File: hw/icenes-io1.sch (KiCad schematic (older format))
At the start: 49 parts, among them J3 Conn_02x11_Odd_Even, U4 iCE40HX8K-CT256, U8 SN74LVC1404, U9 SN74LVC1404, Y1 21.47727MHz, Y2 26.601712MHz

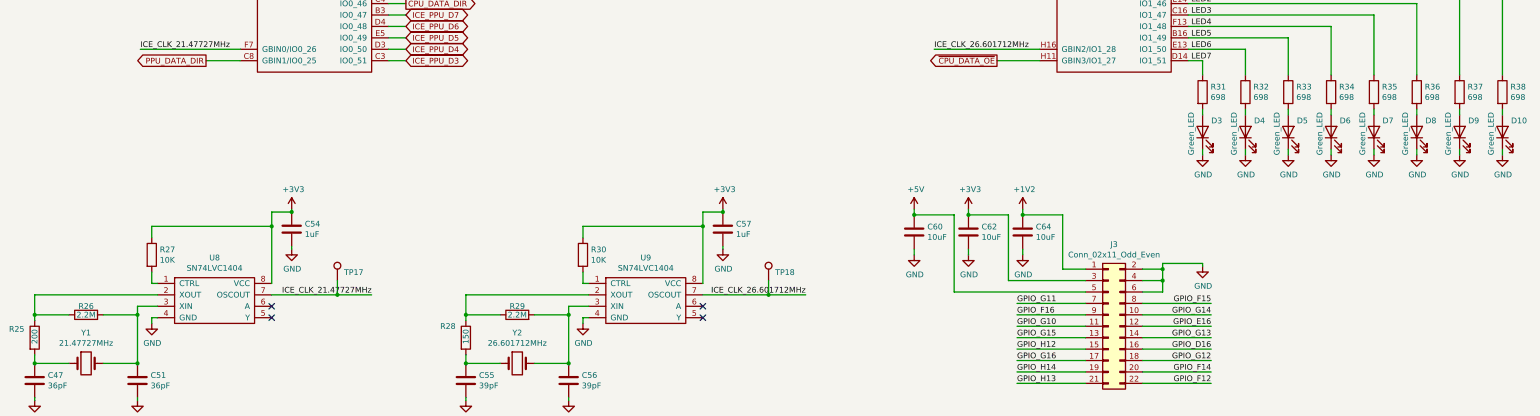
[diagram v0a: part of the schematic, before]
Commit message: Added voltage range in Vin lable (+5V to +10V).
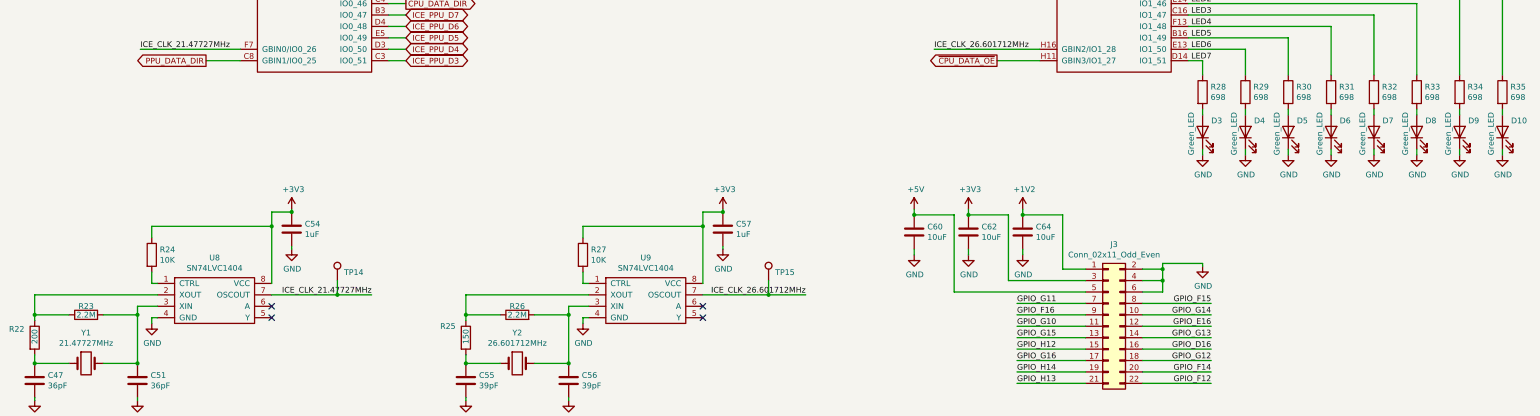
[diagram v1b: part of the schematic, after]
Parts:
- renumbered R25 to R22, R26 to R23, R27 to R24, R28 to R25, R29 to R26, R30 to R27, R31 to R28, R32 to R29, R33 to R30, R34 to R31, R35 to R32, R36 to R33, R37 to R34, R38 to R35, TP17 to TP14, TP18 to TP15
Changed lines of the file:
@@
 $EndComp
 $Comp
-L icenes-library:R698 R31
+L icenes-library:R698 R28
 U 1 1 5D435DC8
 P 11275 7075
-F 0 "R31" V 11229 7145 50  0000 L CNN
+F 0 "R28" V 11229 7145 50  0000 L CNN
 F 1 "R698" H 11275 6975 50  0001 C CNN
 F 2 "Resistor_SMD:R_0603_1608Metric_Pad1.05x0.95mm_HandSolder" V 11275 7075 50  0001 C CNN
@@
 $EndComp
 $Comp
-L icenes-library:R698 R32
+L icenes-library:R698 R29
 U 1 1 5D49EA53
 P 11650 7075
-F 0 "R32" V 11604 7145 50  0000 L CNN
+F 0 "R29" V 11604 7145 50  0000 L CNN
 F 1 "R698" H 11650 6975 50  0001 C CNN
 F 2 "Resistor_SMD:R_0603_1608Metric_Pad1.05x0.95mm_HandSolder" V 11650 7075 50  0001 C CNN
@@
 $EndComp
 $Comp
-L icenes-library:R698 R33
+L icenes-library:R698 R30
 U 1 1 5D4AAC01
 P 12025 7075
-F 0 "R33" V 11979 7145 50  0000 L CNN
+F 0 "R30" V 11979 7145 50  0000 L CNN
 F 1 "R698" H 12025 6975 50  0001 C CNN
 F 2 "Resistor_SMD:R_0603_1608Metric_Pad1.05x0.95mm_HandSolder" V 12025 7075 50  0001 C CNN
@@
 $EndComp
 $Comp
-L icenes-library:R698 R34
+L icenes-library:R698 R31
 U 1 1 5D4B0BF6
 P 12400 7075
-F 0 "R34" V 12354 7145 50  0000 L CNN
+F 0 "R31" V 12354 7145 50  0000 L CNN
 F 1 "R698" H 12400 6975 50  0001 C CNN
 F 2 "Resistor_SMD:R_0603_1608Metric_Pad1.05x0.95mm_HandSolder" V 12400 7075 50  0001 C CNN
@@
 $EndComp
 $Comp
-L icenes-library:R698 R35
+L icenes-library:R698 R32
 U 1 1 5D4B6CEA
 P 12775 7075
-F 0 "R35" V 12729 7145 50  0000 L CNN
+F 0 "R32" V 12729 7145 50  0000 L CNN
 F 1 "R698" H 12775 6975 50  0001 C CNN
 F 2 "Resistor_SMD:R_0603_1608Metric_Pad1.05x0.95mm_HandSolder" V 12775 7075 50  0001 C CNN
@@
 $EndComp
 $Comp
-L icenes-library:R698 R36
+L icenes-library:R698 R33
 U 1 1 5D4BD4B7
 P 13150 7075
-F 0 "R36" V 13104 7145 50  0000 L CNN
+F 0 "R33" V 13104 7145 50  0000 L CNN
 F 1 "R698" H 13150 6975 50  0001 C CNN
 F 2 "Resistor_SMD:R_0603_1608Metric_Pad1.05x0.95mm_HandSolder" V 13150 7075 50  0001 C CNN
@@
 $EndComp
 $Comp
-L icenes-library:R698 R37
+L icenes-library:R698 R34
 U 1 1 5D4C38D7
 P 13525 7075
-F 0 "R37" V 13479 7145 50  0000 L CNN
+F 0 "R34" V 13479 7145 50  0000 L CNN
 F 1 "R698" H 13525 6975 50  0001 C CNN
 F 2 "Resistor_SMD:R_0603_1608Metric_Pad1.05x0.95mm_HandSolder" V 13525 7075 50  0001 C CNN
@@
 $EndComp
 $Comp
-L icenes-library:R698 R38
+L icenes-library:R698 R35
 U 1 1 5D4C971E
 P 13900 7075
-F 0 "R38" V 13854 7145 50  0000 L CNN
+F 0 "R35" V 13854 7145 50  0000 L CNN
 F 1 "R698" H 13900 6975 50  0001 C CNN
 F 2 "Resistor_SMD:R_0603_1608Metric_Pad1.05x0.95mm_HandSolder" V 13900 7075 50  0001 C CNN
@@
 	3125 8250 3125 8750
 $Comp
-L icenes-library:R10K R27
+L icenes-library:R10K R24
 U 1 1 5D74F353
 P 2075 8500
-F 0 "R27" V 2029 8570 50  0000 L CNN
+F 0 "R24" V 2029 8570 50  0000 L CNN
 F 1 "R10K" H 2075 8400 50  0001 C CNN
 F 2 "Resistor_SMD:R_0603_1608Metric_Pad1.05x0.95mm_HandSolder" V 2075 8500 50  0001 C CNN
@@
 Connection ~ 1950 9450
 $Comp
-L icenes-library:R200 R25
+L icenes-library:R200 R22
 U 1 1 5DA45067
 P 1050 9225
-F 0 "R25" V 975 9000 50  0000 L CNN
+F 0 "R22" V 975 9000 50  0000 L CNN
 F 1 "R200" H 1050 9125 50  0001 C CNN
 F 2 "Resistor_SMD:R_0603_1608Metric_Pad1.05x0.95mm_HandSolder" V 1050 9225 50  0001 C CNN
@@
 $EndComp
 $Comp
-L icenes-library:R2.2M R26
+L icenes-library:R2.2M R23
 U 1 1 5DA4708D
 P 1500 9025
-F 0 "R26" H 1500 9100 50  0000 C CNN
+F 0 "R23" H 1500 9100 50  0000 C CNN
 F 1 "R2.2M" H 1500 8925 50  0001 C CNN
 F 2 "Resistor_SMD:R_0603_1608Metric_Pad1.05x0.95mm_HandSolder" V 1500 9025 50  0001 C CNN
@@
 	3700 8850 4000 8850
 $Comp
-L icenes-library:TestPoint TP17
+L icenes-library:TestPoint TP14
 U 1 1 5DB07242
 P 3700 8725
-F 0 "TP17" H 3758 8797 50  0000 L CNN
+F 0 "TP14" H 3758 8797 50  0000 L CNN
 F 1 "TestPoint" H 3700 8925 50  0001 C CNN
 F 2 "TestPoint:TestPoint_Pad_D1.0mm" H 3900 8725 50  0001 C CNN
@@
 	6900 8250 6900 8750
 $Comp
-L icenes-library:R10K R30
+L icenes-library:R10K R27
 U 1 1 5DB221D0
 P 5850 8500
-F 0 "R30" V 5804 8570 50  0000 L CNN
+F 0 "R27" V 5804 8570 50  0000 L CNN
 F 1 "R10K" H 5850 8400 50  0001 C CNN
 F 2 "Resistor_SMD:R_0603_1608Metric_Pad1.05x0.95mm_HandSolder" V 5850 8500 50  0001 C CNN
@@
 Connection ~ 4825 9025
 $Comp
-L icenes-library:R2.2M R29
+L icenes-library:R2.2M R26
 U 1 1 5DB2222B
 P 5275 9025
-F 0 "R29" H 5275 9100 50  0000 C CNN
+F 0 "R26" H 5275 9100 50  0000 C CNN
 F 1 "R2.2M" H 5275 8925 50  0001 C CNN
 F 2 "Resistor_SMD:R_0603_1608Metric_Pad1.05x0.95mm_HandSolder" V 5275 9025 50  0001 C CNN
@@
 Connection ~ 7475 8850
 $Comp
-L icenes-library:TestPoint TP18
+L icenes-library:TestPoint TP15
 U 1 1 5DB22244
 P 7475 8725
-F 0 "TP18" H 7533 8797 50  0000 L CNN
+F 0 "TP15" H 7533 8797 50  0000 L CNN
 F 1 "TestPoint" H 7475 8925 50  0001 C CNN
 F 2 "TestPoint:TestPoint_Pad_D1.0mm" H 7675 8725 50  0001 C CNN
@@
 Connection ~ 5725 9450
 $Comp
-L icenes-library:R150 R28
+L icenes-library:R150 R25
 U 1 1 5DB3EF0F
 P 4825 9225
-F 0 "R28" V 4725 9000 50  0000 L CNN
+F 0 "R25" V 4725 9000 50  0000 L CNN
 F 1 "R150" H 4825 9125 50  0001 C CNN
 F 2 "Resistor_SMD:R_0603_1608Metric_Pad1.05x0.95mm_HandSolder" V 4825 9225 50  0001 C CNN

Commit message: Layout.
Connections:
- net +1V2: now also C60.1, J3.5 (Pin_5); no longer C64.1, J3.1 (Pin_1)
- net +5V: now also C64.1, J3.1 (Pin_1); no longer C60.1, J3.5 (Pin_5)
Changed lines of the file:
@@
 L power:+1V2 #PWR076
 U 1 1 5D76E658
+P 8750 8100
+F 0 "#PWR076" H 8750 7950 50  0001 C CNN
+F 1 "+1V2" H 8765 8273 50  0000 C CNN
+F 2 "" H 8750 8100 50  0001 C CNN
+F 3 "" H 8750 8100 50  0001 C CNN
+	1    8750 8100
+	1    0    0    -1
+$EndComp
+$Comp
+L power:+5V #PWR071
+U 1 1 5D76F52B
 P 9700 8100
-F 0 "#PWR076" H 9700 7950 50  0001 C CNN
-F 1 "+1V2" H 9715 8273 50  0000 C CNN
+F 0 "#PWR071" H 9700 7950 50  0001 C CNN
+F 1 "+5V" H 9715 8273 50  0000 C CNN
 F 2 "" H 9700 8100 50  0001 C CNN
 F 3 "" H 9700 8100 50  0001 C CNN
 	1    9700 8100
-	1    0    0    -1
-$EndComp
-$Comp
-L power:+5V #PWR071
-U 1 1 5D76F52B
-P 8750 8100
-F 0 "#PWR071" H 8750 7950 50  0001 C CNN
-F 1 "+5V" H 8765 8273 50  0000 C CNN
-F 2 "" H 8750 8100 50  0001 C CNN
-F 3 "" H 8750 8100 50  0001 C CNN
-	1    8750 8100
 	1    0    0    -1
 $EndComp
@@
 Wire Wire Line
 	2300 3550 2300 3500
+Text Label 1050 1900 0    50   ~ 0
+VCCIO0_3V3
+Text Label 8050 1900 0    50   ~ 0
+VCCIO1_3V3
+Text Label 1950 3100 0    50   ~ 0
+VCCPLL0_1V2
 $EndSCHEMATC

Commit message: Layout.
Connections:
- net ICE_CLK_21.47727MHz: now also U4.H16 (GBIN2/IO1_28); no longer U4.F7 (GBIN0/IO0_26)
- net ICE_CLK_26.601712MHz: now also U4.F7 (GBIN0/IO0_26); no longer U4.H16 (GBIN2/IO1_28)
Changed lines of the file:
@@
 Connection ~ 3300 8125
 Connection ~ 3125 8250
-Text Label 1975 6700 0    50   ~ 0
+Text Label 8975 6700 0    50   ~ 0
 ICE_CLK_21.47727MHz
 Wire Wire Line
-	1975 6700 2850 6700
+	8975 6700 9850 6700
 Wire Wire Line
 	1050 8850 2125 8850
@@
 Wire Wire Line
 	7475 8850 7800 8850
-Text Label 8925 6700 0    50   ~ 0
+Text Label 1925 6700 0    50   ~ 0
 ICE_CLK_26.601712MHz
 Wire Wire Line
-	8925 6700 9850 6700
-Text GLabel 2550 6800 0    50   Output ~ 0
+	1925 6700 2850 6700
+Text GLabel 2500 6800 0    50   Output ~ 0
 PPU_DATA_DIR
-Wire Wire Line
-	2550 6800 2850 6800
-Text GLabel 9475 6800 0    50   Output ~ 0
+Text GLabel 9525 6800 0    50   Output ~ 0
 ~CPU_DATA_OE
-Wire Wire Line
-	9475 6800 9850 6800
 $Comp
 L power:PWR_FLAG #FLG?
@@
 Text Label 1950 3100 0    50   ~ 0
 VCCPLL0_1V2
+Wire Wire Line
+	2500 6800 2850 6800
+Wire Wire Line
+	9850 6800 9525 6800
 $EndSCHEMATC

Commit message: Layout.
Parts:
- removed C60, C62, C64: C10uF, Capacitor_SMD:C_0603_1608Metric_Pad1.05x0.95mm_HandSolder, symbol icenes-library:C10uF
- removed J3: Conn_02x11_Odd_Even, Connector_PinSocket_2.54mm:PinSocket_2x11_P2.54mm_Vertical, symbol icenes-library:Conn_02x11_Odd_Even
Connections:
- net CTSn is gone; now on net ~PPU_DATA_OE: U4.B14 (IO0_03)
- net DCDn is gone; now on net PPU_ADDR_DIR: U4.C13 (IO0_06)
- net DSRn is gone; now on net LED2: U4.E11 (IO0_05)
- net DTRn is gone; now on net ~PPU_ADDR_OE: U4.C12 (IO0_04)
- net GPIO_D16 is gone; now on net ICE_CPU_D2: U4.D16 (IO1_40)
- net GPIO_E16 is gone; now on net ICE_CPU_D1: U4.E16 (IO1_38)
- net GPIO_F12 is gone; now on net ICE_M2: U4.F12 (IO1_43)
- net GPIO_F14 is gone; now on net CPU_DATA_DIR: U4.F14 (IO1_42)
- net GPIO_F15 is gone; now on net ICE_CIRAM_A10: U4.F15 (IO1_36)
- net GPIO_F16 is gone; now on net ICE_CPU_D0: U4.F16 (IO1_34)
- net GPIO_G10 is gone; now on net ICE_PPU_D3: U4.G10 (IO1_33)
- net GPIO_G11 is gone; now on net ICE_PPU_D2: U4.G11 (IO1_35)
- net GPIO_G12 is gone; now on net ICE_SYSTEM_CLK: U4.G12 (IO1_41)
- net GPIO_G13 is gone; now on net ICE_CICtoPak: U4.G13 (IO1_39)
- net GPIO_G15 is gone; now on net ~ICE_CIRAM_CE: U4.G15 (IO1_32)
- net GPIO_G16 is gone; now on net ~CPU_DATA_OE: U4.G16 (IO1_30)
- net GPIO_H13 is gone; now on net ICE_CIC_CLK: U4.H13 (IO1_26)
- net GPIO_H14 is gone; now on net ~ICE_IRQ: U4.H14 (IO1_29)
- net RS232_RX_TTL is gone; now on net ICE_PPU_D1: U4.C14 (IO0_00)
- net RS232_TX_TTL is gone; now on net ICE_PPU_D0: U4.B15 (IO0_01)
- net RTSn is gone; now on net LED1: U4.D13 (IO0_02)
- net CPU_ADDR_DIR: now also U4.D7 (IO0_35); no longer U4.D8 (IO0_28)
- net CPU_DATA_DIR: no longer U4.C4 (IO0_46)
- net ICE_CIC_CLK: no longer U4.K13 (IO1_17)
- net ICE_CICtoMB: now also U4.E13 (IO1_50); no longer U4.J14 (IO1_22)
- net ICE_CICtoPak: no longer U4.K14 (IO1_18)
- net ICE_CIRAM_A10: no longer U4.J16 (IO1_25)
- net ICE_CPU_A0: now also U4.B8 (IO0_29); no longer U4.A1 (IO0_44)
- net ICE_CPU_A1: now also U4.B7 (IO0_32); no longer U4.D5 (IO0_43)
- net ICE_CPU_A10: now also U4.B5 (IO0_39); no longer U4.C6 (IO0_34)
- net ICE_CPU_A11: now also U4.C3 (IO0_51); no longer U4.B6 (IO0_33)
- net ICE_CPU_A12: now also U4.B4 (IO0_41); no longer U4.B7 (IO0_32)
- net ICE_CPU_A13: now also U4.A2 (IO0_42); no longer U4.C7 (IO0_31)
- net ICE_CPU_A14: now also U4.D3 (IO0_50); no longer U4.A7 (IO0_30)
- net ICE_CPU_A2: now also U4.D6 (IO0_37); no longer U4.A2 (IO0_42)
- net ICE_CPU_A3: now also U4.A7 (IO0_30); no longer U4.B4 (IO0_41)
- net ICE_CPU_A4: now also U4.B6 (IO0_33); no longer U4.E6 (IO0_40)
- net ICE_CPU_A5: now also U4.C5 (IO0_45); no longer U4.B5 (IO0_39)
- net ICE_CPU_A6: now also U4.C4 (IO0_46); no longer U4.A5 (IO0_38)
- net ICE_CPU_A7: now also U4.A6 (IO0_36); no longer U4.D6 (IO0_37)
- net ICE_CPU_A8: now also U4.B3 (IO0_47); no longer U4.A6 (IO0_36)
- net ICE_CPU_A9: now also U4.A5 (IO0_38); no longer U4.D7 (IO0_35)
- net ICE_CPU_D0: no longer U4.L14 (IO1_10)
- net ICE_CPU_D1: no longer U4.L13 (IO1_09)
- net ICE_CPU_D2: no longer U4.N16 (IO1_08)
- net ICE_CPU_D3: now also U4.E14 (IO1_46); no longer U4.L12 (IO1_07)
- net ICE_CPU_D4: now also U4.D14 (IO1_51); no longer U4.M14 (IO1_06)
- net ICE_CPU_D5: now also U4.D15 (IO1_44); no longer U4.M13 (IO1_05)
- net ICE_CPU_D6: now also U4.C16 (IO1_47); no longer U4.P16 (IO1_04)
- net ICE_CPU_D7: now also U4.B16 (IO1_49); no longer U4.P15 (IO1_03)
- net ICE_CPU_RW: now also U4.A1 (IO0_44); no longer U4.B8 (IO0_29)
- net ICE_M2: no longer U4.M15 (IO1_14)
- net ICE_PPU_A0: now also U4.B12 (IO0_13); no longer U4.E10 (IO0_10)
- net ICE_PPU_A1: now also U4.B11 (IO0_15); no longer U4.C11 (IO0_11)
- net ICE_PPU_A11: now also U4.B9 (IO0_27); no longer U4.E9 (IO0_21)
- net ICE_PPU_A2: now also U4.E9 (IO0_21); no longer U4.D11 (IO0_12)
- net ICE_PPU_A3: now also U4.D8 (IO0_28); no longer U4.B12 (IO0_13)
- net ICE_PPU_A4: now also U4.E6 (IO0_40); no longer U4.B10 (IO0_14)
- net ICE_PPU_A5: now also U4.C11 (IO0_11); no longer U4.B11 (IO0_15)
- net ICE_PPU_A7: now also U4.A11 (IO0_18); no longer U4.A10 (IO0_17)
- net ICE_PPU_A8: now also U4.B10 (IO0_14); no longer U4.A11 (IO0_18)
- net ICE_PPU_A9: now also U4.A10 (IO0_17); no longer U4.D10 (IO0_19)
- net ICE_PPU_D0: no longer U4.P14 (IO1_02)
- net ICE_PPU_D1: no longer U4.R15 (IO1_01)
- net ICE_PPU_D2: no longer U4.R14 (IO1_00)
- net ICE_PPU_D3: no longer U4.C3 (IO0_51)
- net ICE_PPU_D4: now also U4.E10 (IO0_10); no longer U4.D3 (IO0_50)
- net ICE_PPU_D5: now also U4.F9 (IO0_24); no longer U4.E5 (IO0_49)
- net ICE_PPU_D6: now also U4.A16 (IO0_07); no longer U4.D4 (IO0_48)
- net ICE_PPU_D7: now also U4.A15 (IO0_08); no longer U4.B3 (IO0_47)
- net ICE_SYSTEM_CLK: no longer U4.J10 (IO1_13)
- net LED0: now also U4.F11 (IO1_45); no longer U4.D15 (IO1_44)
- net LED1: no longer U4.F11 (IO1_45)
- net LED2: no longer U4.E14 (IO1_46)
- net LED3: now also U4.D11 (IO0_12); no longer U4.C16 (IO1_47)
- net LED4: now also U4.D10 (IO0_19); no longer U4.F13 (IO1_48)
- net LED5: now also U4.E5 (IO0_49); no longer U4.B16 (IO1_49)
- net LED6: now also U4.D5 (IO0_43); no longer U4.E13 (IO1_50)
- net LED7: now also U4.D4 (IO0_48); no longer U4.D14 (IO1_51)
- net MISC_DIR2: now also U4.J16 (IO1_25); no longer U4.K16 (IO1_21)
- net PPU_ADDR_DIR: no longer U4.A15 (IO0_08)
- net PPU_DATA_DIR: now also U4.B13 (IO0_09); no longer U4.C8 (GBIN1/IO0_25)
- net ~CPU_ADDR_OE: now also U4.C6 (IO0_34); no longer U4.B9 (IO0_27)
- net ~CPU_DATA_OE: no longer U4.H11 (GBIN3/IO1_27)
- net ~ICE_CIC_RST: now also U4.F13 (IO1_48); no longer U4.J15 (IO1_19)
- net ~ICE_CIRAM_CE: no longer U4.J13 (IO1_24)
- net ~ICE_IRQ: no longer U4.J12 (IO1_23)
- net ~ICE_PPU_A13: now also U4.C8 (GBIN1/IO0_25); no longer U4.F9 (IO0_24)
- net ~ICE_PPU_RD: now also U4.K15 (IO1_20); no longer U4.J11 (IO1_15)
- net ~ICE_PPU_WR: now also U4.C7 (IO0_31); no longer U4.B13 (IO0_09)
- net ~ICE_ROMSEL: now also U4.K16 (IO1_21); no longer U4.L16 (IO1_16)
- net ~MISC_OE1: now also U4.L16 (IO1_16); no longer U4.K12 (IO1_11)
- net ~MISC_OE2: now also U4.J15 (IO1_19); no longer U4.K15 (IO1_20)
- net ~PPU_ADDR_OE: no longer U4.A16 (IO0_07)
- net ~PPU_DATA_OE: no longer U4.C5 (IO0_45)
- net GPIO_H12 renamed GPIO_E13
- new net GPIO_C10: U4.J10 (IO1_13)
- new net GPIO_H11: U4.H11 (GBIN3/IO1_27)
- new net GPIO_J11: U4.J11 (IO1_15)
- new net GPIO_J12: U4.J12 (IO1_23)
- new net GPIO_J13: U4.J13 (IO1_24)
- new net GPIO_J14: U4.J14 (IO1_22)
- new net GPIO_K12: U4.K12 (IO1_11)
- new net GPIO_K13: U4.K13 (IO1_17)
- new net GPIO_K14: U4.K14 (IO1_18)
- new net GPIO_L12: U4.L12 (IO1_07)
- new net GPIO_L13: U4.L13 (IO1_09)
- new net GPIO_M13: U4.M13 (IO1_05)
- new net GPIO_M14: U4.M14 (IO1_06)
- new net GPIO_M15: U4.M15 (IO1_14)
- new net GPIO_M16: U4.L14 (IO1_10)
- new net GPIO_N16: U4.N16 (IO1_08)
- new net GPIO_P14: U4.P14 (IO1_02)
- new net GPIO_P15: U4.P15 (IO1_03)
- new net GPIO_P16: U4.P16 (IO1_04)
- new net GPIO_R14: U4.R14 (IO1_00)
- new net GPIO_R15: U4.R15 (IO1_01)
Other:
- moved on the sheet: D10, D3, D4, D5, D6, D7, D8, D9, R28, R29, R30, R31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

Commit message: Layout. Added some info for the PAL crystal.
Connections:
- net GPIO_E13 renamed GPIO_H12
- net GPIO_M16 renamed GPIO_L14
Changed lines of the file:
@@
 Text Label 4750 6000 2    50   ~ 0
 LED6
-Text Label 12075 2300 2    50   ~ 0
-GPIO_P16
 Text Label 5125 3100 2    50   ~ 0
 LED3
 Text Label 11750 5400 2    50   ~ 0
 GPIO_G14
-Text Label 11750 3000 2    50   ~ 0
-GPIO_K12
-Text Label 11750 2400 2    50   ~ 0
-GPIO_M13
-Text Label 11750 2600 2    50   ~ 0
-GPIO_L12
-Text Label 11750 4100 2    50   ~ 0
-GPIO_J14
-Text Label 11750 3600 2    50   ~ 0
-GPIO_K13
-Text Label 11750 4200 2    50   ~ 0
-GPIO_J12
 Text GLabel 12000 5300 2    50   Input ~ 0
 ICE_CIRAM_A10
@@
 Wire Wire Line
 	11150 4800 11750 4800
-Text Label 11750 3300 2    50   ~ 0
-GPIO_M15
 Text Label 11750 6200 2    50   ~ 0
 LED0
-Text Label 11750 4300 2    50   ~ 0
-GPIO_J13
 Text Label 11750 3200 2    50   ~ 0
 GPIO_C10
-Text Label 11750 3700 2    50   ~ 0
-GPIO_K14
-Text Label 11750 2900 2    50   ~ 0
-GPIO_M16
-Text Label 11750 4800 2    50   ~ 0
-GPIO_E13
 Wire Wire Line
 	11150 3400 11750 3400
-Text Label 11750 3400 2    50   ~ 0
-GPIO_J11
 Wire Wire Line
 	4150 5000 4300 5000
@@
 Wire Wire Line
 	11150 2800 11750 2800
-Text Label 11750 2800 2    50   ~ 0
+Wire Wire Line
+	11150 2700 11750 2700
+Wire Wire Line
+	11150 2500 11750 2500
+Wire Wire Line
+	11150 1900 11750 1900
+Wire Wire Line
+	11150 2200 11750 2200
+Wire Wire Line
+	11150 2000 11750 2000
+Wire Wire Line
+	11150 2100 11750 2100
+Text GLabel 11750 3400 2    50   BiDi ~ 0
+GPIO_J11
+Text GLabel 11750 3000 2    50   BiDi ~ 0
+GPIO_K12
+Text GLabel 11750 2800 2    50   BiDi ~ 0
 GPIO_L13
-Wire Wire Line
-	11150 2700 11750 2700
-Text Label 11750 2700 2    50   ~ 0
+Text GLabel 11750 2600 2    50   BiDi ~ 0
+GPIO_L12
+Text GLabel 11750 3300 2    50   BiDi ~ 0
+GPIO_M15
+Text GLabel 11750 2700 2    50   BiDi ~ 0
 GPIO_N16
-Wire Wire Line
-	11150 2500 11750 2500
-Text Label 11750 2500 2    50   ~ 0
+Text GLabel 12075 2300 2    50   BiDi ~ 0
+GPIO_P16
+Text GLabel 11750 2200 2    50   BiDi ~ 0
+GPIO_P15
+Text GLabel 11750 2000 2    50   BiDi ~ 0
+GPIO_R15
+Text GLabel 11750 4800 2    50   BiDi ~ 0
+GPIO_H12
+Text GLabel 11750 4100 2    50   BiDi ~ 0
+GPIO_J14
+Text GLabel 11750 4300 2    50   BiDi ~ 0
+GPIO_J13
+Text GLabel 11750 4200 2    50   BiDi ~ 0
+GPIO_J12
+Text GLabel 11750 3700 2    50   BiDi ~ 0
+GPIO_K14
+Text GLabel 11750 3600 2    50   BiDi ~ 0
+GPIO_K13
+Text GLabel 11750 2900 2    50   BiDi ~ 0
+GPIO_L14
+Text GLabel 11750 2500 2    50   BiDi ~ 0
 GPIO_M14
-Wire Wire Line
-	11150 1900 11750 1900
-Text Label 11750 1900 2    50   ~ 0
+Text GLabel 11750 2400 2    50   BiDi ~ 0
+GPIO_M13
+Text GLabel 11750 2100 2    50   BiDi ~ 0
+GPIO_P14
+Text GLabel 11750 1900 2    50   BiDi ~ 0
 GPIO_R14
-Wire Wire Line
-	11150 2200 11750 2200
-Text Label 11750 2200 2    50   ~ 0
-GPIO_P15
-Wire Wire Line
-	11150 2000 11750 2000
-Text Label 11750 2000 2    50   ~ 0
-GPIO_R15
-Wire Wire Line
-	11150 2100 11750 2100
-Text Label 11750 2100 2    50   ~ 0
-GPIO_P14
 $EndSCHEMATC

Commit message: Layout.
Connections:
- net GPIO_C10 renamed GPIO_J10
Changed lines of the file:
@@
 Text Label 5125 3100 2    50   ~ 0
 LED3
-Text Label 11750 5400 2    50   ~ 0
-GPIO_G14
 Text GLabel 12000 5300 2    50   Input ~ 0
 ICE_CIRAM_A10
@@
 Wire Wire Line
 	8975 6800 9850 6800
-Text Label 8975 6800 0    50   ~ 0
-GPIO_H11
 Wire Wire Line
 	4150 3100 5125 3100
@@
 Text Label 11750 6200 2    50   ~ 0
 LED0
-Text Label 11750 3200 2    50   ~ 0
-GPIO_C10
 Wire Wire Line
 	11150 3400 11750 3400
@@
 Text GLabel 11750 1900 2    50   BiDi ~ 0
 GPIO_R14
+Text GLabel 11750 5400 2    50   BiDi ~ 0
+GPIO_G14
+Text GLabel 8975 6800 0    50   BiDi ~ 0
+GPIO_H11
+Text GLabel 11750 3200 2    50   BiDi ~ 0
+GPIO_J10
 $EndSCHEMATC
